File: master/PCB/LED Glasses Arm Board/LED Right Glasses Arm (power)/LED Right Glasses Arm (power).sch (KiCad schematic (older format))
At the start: 24 parts, among them J1 Conn_01x02_Male, J2 Conn_01x01_Male, J3 Conn_01x01_Male, Q1 TP0610T, SW1 SW_SPST, U1 TPS63060

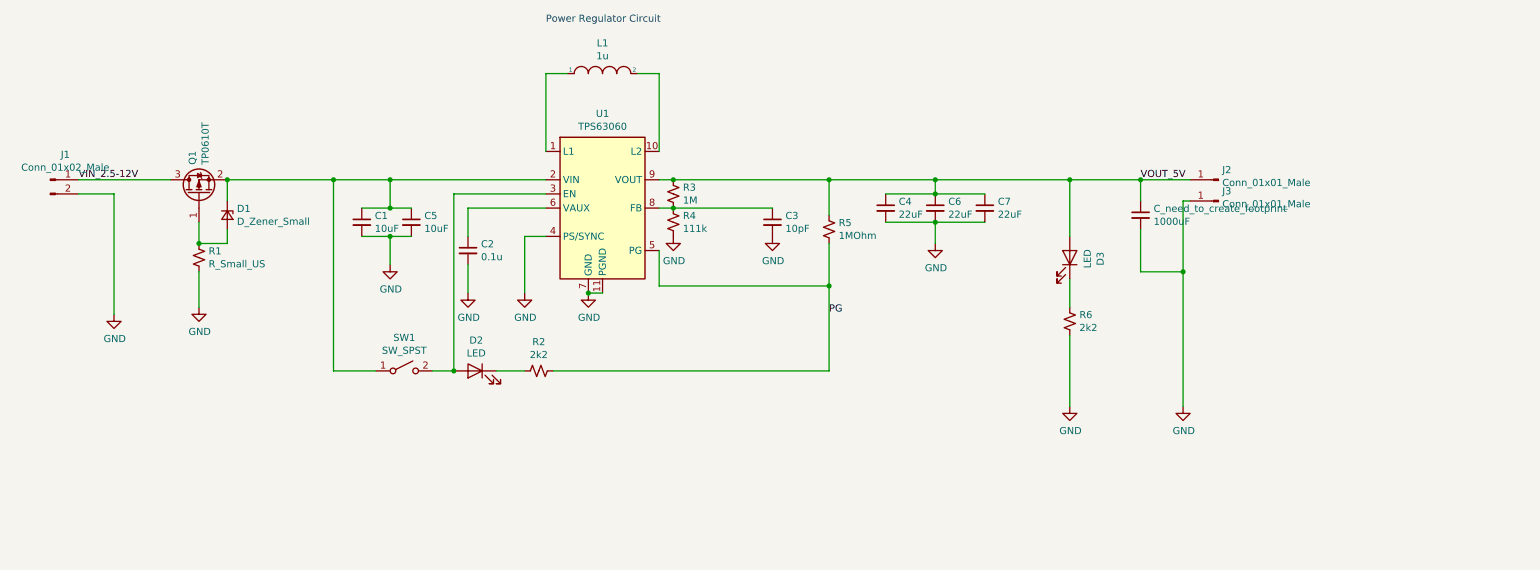
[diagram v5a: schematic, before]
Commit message: PCB update
Changed mosfet, started to route signals
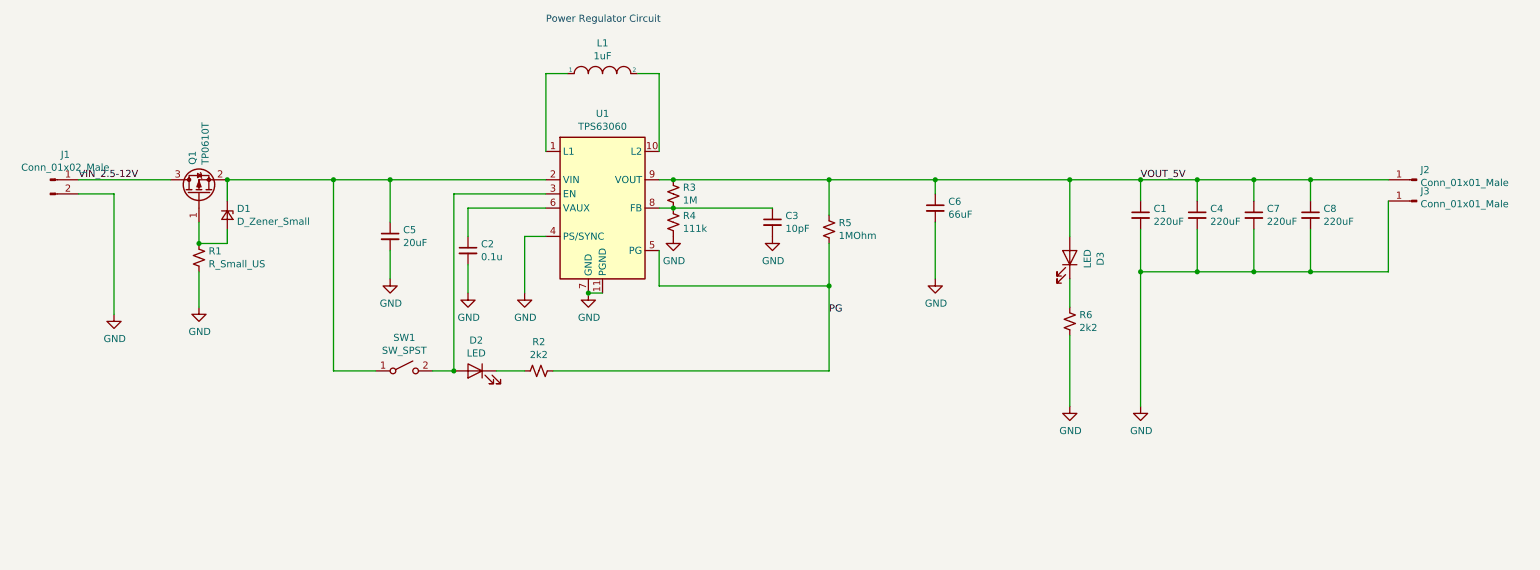
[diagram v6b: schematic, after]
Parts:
- removed C1: 10uF, Capacitor_SMD:C_0603_1608Metric, symbol Device:C_Small
- added C8: 220uF, Capacitor_SMD:C_1206_3216Metric, symbol Device:C_Small
- C1: renamed from C_need_to_create_footprint; value 1000uF -> 220uF; footprint Capacitor_SMD:C_0603_1608Metric -> Capacitor_SMD:C_1206_3216Metric; Link https://www.digikey.com.au/product-detail/en/vishay-sprague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 -> https://au.element14.com/murata/grm31cr60j227me11l/cap-220-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
- C4, C7: value 22uF -> 220uF; footprint Capacitor_SMD:C_0603_1608Metric -> Capacitor_SMD:C_1206_3216Metric; Link (none) -> https://au.element14.com/murata/grm31cr60j227me11l/cap-220-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
- C5: value 10uF -> 20uF
- C6: value 22uF -> 66uF
- J1: footprint Connector_JST:JST_PH_S2B-PH-K_1x02_P2.00mm_Horizontal -> Connector_JST:JST_PH_S2B-PH-SM4-TB_1x02-1MP_P2.00mm_Horizontal; Link (none) -> https://au.element14.com/jst-japan-solderless-terminals/s2b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
- L1: value 1u -> 1uF; Link (none) -> XFL4020-102MEC
- Q1: Link (none) -> https://au.element14.com/vishay/si2315bds-t1-ge3/p-channel-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
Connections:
- net GND: now also C8.2
- net VOUT_5V: now also C8.1
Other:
- moved on the sheet: C5, J2, J3
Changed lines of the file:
@@
-$EndComp
-$Comp
-L Device:C_Small C1
-U 1 1 5F4B72C8
-P 3050 4350
-F 0 "C1" H 3142 4396 50  0000 L CNN
-F 1 "10uF" H 3142 4305 50  0000 L CNN
-F 2 "Capacitor_SMD:C_0603_1608Metric" H 3050 4350 50  0001 C CNN
-F 3 "~" H 3050 4350 50  0001 C CNN
-	1    3050 4350
-	1    0    0    -1
 $EndComp
 $Comp
@@
 P 4750 3300
 F 0 "L1" H 4750 3515 50  0000 C CNN
-F 1 "1u" H 4750 3424 50  0000 C CNN
+F 1 "1uF" H 4750 3424 50  0000 C CNN
 F 2 "Inductor_SMD:L_Coilcraft_XxL4020" H 4750 3300 50  0001 C CNN
-F 3 "~" H 4750 3300 50  0001 C CNN
+F 3 "http://www.farnell.com/datasheets/1682010.pdf" H 4750 3300 50  0001 C CNN
+F 4 "XFL4020-102MEC" H 4750 3300 50  0001 C CNN "Link"
 	1    4750 3300
 	1    0    0    -1
@@
 Connection ~ 6350 4050
 $Comp
-L Device:C_Small C4
-U 1 1 5F4BC943
-P 6750 4250
-F 0 "C4" H 6842 4296 50  0000 L CNN
-F 1 "22uF" H 6842 4205 50  0000 L CNN
-F 2 "Capacitor_SMD:C_0603_1608Metric" H 6750 4250 50  0001 C CNN
-F 3 "~" H 6750 4250 50  0001 C CNN
-	1    6750 4250
-	1    0    0    -1
-$EndComp
-$Comp
 L power:GND #PWR0108
 U 1 1 5F4BEA89
-P 7100 4500
-F 0 "#PWR0108" H 7100 4250 50  0001 C CNN
-F 1 "GND" H 7105 4327 50  0000 C CNN
-F 2 "" H 7100 4500 50  0001 C CNN
-F 3 "" H 7100 4500 50  0001 C CNN
-	1    7100 4500
+P 7100 4750
+F 0 "#PWR0108" H 7100 4500 50  0001 C CNN
+F 1 "GND" H 7105 4577 50  0000 C CNN
+F 2 "" H 7100 4750 50  0001 C CNN
+F 3 "" H 7100 4750 50  0001 C CNN
+	1    7100 4750
 	1    0    0    -1
 $EndComp
@@
 F 1 "TP0610T" H 2106 4105 50  0000 L CNN
 F 2 "Package_TO_SOT_SMD:SOT-23" H 2100 4075 50  0001 L CIN
-F 3 "http://www.vishay.com/docs/70209/70209.pdf" H 1900 4150 50  0001 L CNN
+F 3 "http://www.farnell.com/datasheets/2046951.pdf" H 1900 4150 50  0001 L CNN
+F 4 "https://au.element14.com/vishay/si2315bds-t1-ge3/p-channel-mosfet/dp/1867177?st=p%20channel%20mosfet" H 1900 4150 50  0001 C CNN "Link"
 	1    1900 4150
 	0    -1   -1   0
@@
 L Device:C_Small C5
 U 1 1 604D825D
-P 3400 4350
-F 0 "C5" H 3492 4396 50  0000 L CNN
-F 1 "10uF" H 3492 4305 50  0000 L CNN
-F 2 "Capacitor_SMD:C_0603_1608Metric" H 3400 4350 50  0001 C CNN
-F 3 "~" H 3400 4350 50  0001 C CNN
-	1    3400 4350
+P 3250 4450
+F 0 "C5" H 3342 4496 50  0000 L CNN
+F 1 "20uF" H 3342 4405 50  0000 L CNN
+F 2 "Capacitor_SMD:C_0603_1608Metric" H 3250 4450 50  0001 C CNN
+F 3 "~" H 3250 4450 50  0001 C CNN
+	1    3250 4450
 	1    0    0    -1
 $EndComp
@@
 Wire Wire Line
 	8050 4050 8550 4050
-$Comp
-L Device:C_Small C7
-U 1 1 604E036B
-P 7450 4250
-F 0 "C7" H 7542 4296 50  0000 L CNN
-F 1 "22uF" H 7542 4205 50  0000 L CNN
-F 2 "Capacitor_SMD:C_0603_1608Metric" H 7450 4250 50  0001 C CNN
-F 3 "~" H 7450 4250 50  0001 C CNN
-	1    7450 4250
-	1    0    0    -1
-$EndComp
 $Comp
 L Device:C_Small C6
@@
 P 7100 4250
 F 0 "C6" H 7192 4296 50  0000 L CNN
-F 1 "22uF" H 7192 4205 50  0000 L CNN
+F 1 "66uF" H 7192 4205 50  0000 L CNN
 F 2 "Capacitor_SMD:C_0603_1608Metric" H 7100 4250 50  0001 C CNN
 F 3 "~" H 7100 4250 50  0001 C CNN
@@
 Wire Wire Line
 	7100 4050 8050 4050
-Wire Wire Line
-	7100 4350 7100 4500
 $Comp
 L Connector:Conn_01x02_Male J1
@@
 F 0 "J1" H 956 4228 50  0000 C CNN
 F 1 "Conn_01x02_Male" H 956 4137 50  0000 C CNN
-F 2 "Connector_JST:JST_PH_S2B-PH-K_1x02_P2.00mm_Horizontal" H 850 4050 50  0001 C CNN
-F 3 "~" H 850 4050 50  0001 C CNN
+F 2 "Connector_JST:JST_PH_S2B-PH-SM4-TB_1x02-1MP_P2.00mm_Horizontal" H 850 4050 50  0001 C CNN
+F 3 "http://www.farnell.com/datasheets/1699381.pdf" H 850 4050 50  0001 C CNN
+F 4 "https://au.element14.com/jst-japan-solderless-terminals/s2b-ph-sm4-tb-lf-sn/connector-header-smt-r-a-2mm-2way/dp/9492615" H 850 4050 50  0001 C CNN "Link"
 	1    850  4050
 	1    0    0    -1
@@
 L Connector:Conn_01x01_Male J2
 U 1 1 604D92F9
-P 9100 4050
-F 0 "J2" H 9073 3980 50  0000 R CNN
-F 1 "Conn_01x01_Male" H 9073 4071 50  0000 R CNN
-F 2 "Connector_PinHeader_1.00mm:PinHeader_1x01_P1.00mm_Vertical_SMD_CUSTOM" H 9100 4050 50  0001 C CNN
-F 3 "~" H 9100 4050 50  0001 C CNN
-	1    9100 4050
+P 10500 4050
+F 0 "J2" H 10473 3980 50  0000 R CNN
+F 1 "Conn_01x01_Male" H 10473 4071 50  0000 R CNN
+F 2 "Connector_PinHeader_1.00mm:PinHeader_1x01_P1.00mm_Vertical_SMD_CUSTOM" H 10500 4050 50  0001 C CNN
+F 3 "~" H 10500 4050 50  0001 C CNN
+	1    10500 4050
 	-1   0    0    1
 $EndComp
@@
 L power:GND #PWR0111
 U 1 1 604DB74C
-P 8850 5650
-F 0 "#PWR0111" H 8850 5400 50  0001 C CNN
-F 1 "GND" H 8855 5477 50  0000 C CNN
-F 2 "" H 8850 5650 50  0001 C CNN
-F 3 "" H 8850 5650 50  0001 C CNN
-	1    8850 5650
+P 8550 5650
+F 0 "#PWR0111" H 8550 5400 50  0001 C CNN
+F 1 "GND" H 8555 5477 50  0000 C CNN
+F 2 "" H 8550 5650 50  0001 C CNN
+F 3 "" H 8550 5650 50  0001 C CNN
+	1    8550 5650
 	1    0    0    -1
 $EndComp
@@
 L Connector:Conn_01x01_Male J3
 U 1 1 604DC290
-P 9100 4200
-F 0 "J3" H 9073 4130 50  0000 R CNN
-F 1 "Conn_01x01_Male" H 9073 4221 50  0000 R CNN
-F 2 "Connector_PinHeader_1.00mm:PinHeader_1x01_P1.00mm_Vertical_SMD_CUSTOM" H 9100 4200 50  0001 C CNN
-F 3 "~" H 9100 4200 50  0001 C CNN
-	1    9100 4200
+P 10500 4200
+F 0 "J3" H 10473 4130 50  0000 R CNN
+F 1 "Conn_01x01_Male" H 10473 4221 50  0000 R CNN
+F 2 "Connector_PinHeader_1.00mm:PinHeader_1x01_P1.00mm_Vertical_SMD_CUSTOM" H 10500 4200 50  0001 C CNN
+F 3 "~" H 10500 4200 50  0001 C CNN
+	1    10500 4200
 	-1   0    0    1
 $EndComp
 Wire Wire Line
-	8900 4200 8850 4200
-Wire Wire Line
-	8850 4200 8850 4700
-Wire Wire Line
-	3050 4250 3250 4250
-Connection ~ 3250 4250
-Wire Wire Line
-	3250 4250 3400 4250
-Wire Wire Line
 	2850 4050 3250 4050
-Wire Wire Line
-	3050 4450 3250 4450
 $Comp
 L power:GND #PWR0103
 U 1 1 5F4B6F97
-P 3250 4650
-F 0 "#PWR0103" H 3250 4400 50  0001 C CNN
-F 1 "GND" H 3255 4477 50  0000 C CNN
-F 2 "" H 3250 4650 50  0001 C CNN
-F 3 "" H 3250 4650 50  0001 C CNN
-	1    3250 4650
-	1    0    0    -1
-$EndComp
-Wire Wire Line
-	3250 4050 3250 4250
+P 3250 4750
+F 0 "#PWR0103" H 3250 4500 50  0001 C CNN
+F 1 "GND" H 3255 4577 50  0000 C CNN
+F 2 "" H 3250 4750 50  0001 C CNN
+F 3 "" H 3250 4750 50  0001 C CNN
+	1    3250 4750
+	1    0    0    -1
+$EndComp
 Connection ~ 3250 4050
 Wire Wire Line
 	3250 4050 4350 4050
 Wire Wire Line
-	3250 4450 3250 4650
-Connection ~ 3250 4450
-Wire Wire Line
-	3250 4450 3400 4450
-Wire Wire Line
-	6750 4350 7100 4350
-Connection ~ 7100 4350
-Wire Wire Line
-	7100 4350 7450 4350
-Wire Wire Line
-	6750 4150 7100 4150
-Connection ~ 7100 4150
-Wire Wire Line
-	7100 4150 7450 4150
-$Comp
-L Device:C_Small C_need_to_create_footprint
+	3250 4550 3250 4750
+$Comp
+L Device:C_Small C1
 U 1 1 60505078
 P 8550 4300
-F 0 "C_need_to_create_footprint" H 8642 4346 50  0000 L CNN
-F 1 "1000uF" H 8642 4255 50  0000 L CNN
-F 2 "Capacitor_SMD:C_0603_1608Metric" H 8550 4300 50  0001 C CNN
-F 3 "https://www.vishay.com/docs/40012/591d.pdf" H 8550 4300 50  0001 C CNN
-F 4 "https://www.digikey.com.au/product-detail/en/vishay-sprague/591D108X96R3R2T20H/718-1619-1-ND/1973897" H 8550 4300 50  0001 C CNN "Link"
+F 0 "C1" H 8642 4346 50  0000 L CNN
+F 1 "220uF" H 8642 4255 50  0000 L CNN
+F 2 "Capacitor_SMD:C_1206_3216Metric" H 8550 4300 50  0001 C CNN
+F 3 "http://www.farnell.com/datasheets/2867879.pdf" H 8550 4300 50  0001 C CNN
+F 4 "https://au.element14.com/murata/grm31cr60j227me11l/cap-220-f-6-3v-20-x5r-1206/dp/2494472" H 8550 4300 50  0001 C CNN "Link"
 	1    8550 4300
 	1    0    0    -1
@@
 Connection ~ 8550 4050
 Wire Wire Line
-	8550 4050 8900 4050
-Wire Wire Line
 	8550 4400 8550 4700
 Wire Wire Line
-	8550 4700 8850 4700
-Connection ~ 8850 4700
-Wire Wire Line
-	8850 4700 8850 5650
+	8550 4700 8550 5650
+Wire Wire Line
+	3250 4050 3250 4350
+Wire Wire Line
+	7100 4350 7100 4750
+Wire Wire Line
+	10300 4700 10300 4200
+Connection ~ 8550 4700
+$Comp
+L Device:C_Small C4
+U 1 1 60562E44
+P 8950 4300
+F 0 "C4" H 9042 4346 50  0000 L CNN
+F 1 "220uF" H 9042 4255 50  0000 L CNN
+F 2 "Capacitor_SMD:C_1206_3216Metric" H 8950 4300 50  0001 C CNN
+F 3 "http://www.farnell.com/datasheets/2867879.pdf" H 8950 4300 50  0001 C CNN
+F 4 "https://au.element14.com/murata/grm31cr60j227me11l/cap-220-f-6-3v-20-x5r-1206/dp/2494472" H 8950 4300 50  0001 C CNN "Link"
+	1    8950 4300
+	1    0    0    -1
+$EndComp
+$Comp
+L Device:C_Small C7
+U 1 1 605639D8
+P 9350 4300
+F 0 "C7" H 9442 4346 50  0000 L CNN
+F 1 "220uF" H 9442 4255 50  0000 L CNN
+F 2 "Capacitor_SMD:C_1206_3216Metric" H 9350 4300 50  0001 C CNN
+F 3 "http://www.farnell.com/datasheets/2867879.pdf" H 9350 4300 50  0001 C CNN
+F 4 "https://au.element14.com/murata/grm31cr60j227me11l/cap-220-f-6-3v-20-x5r-1206/dp/2494472" H 9350 4300 50  0001 C CNN "Link"
+	1    9350 4300
+	1    0    0    -1
+$EndComp
+$Comp
+L Device:C_Small C8
+U 1 1 60564591
+P 9750 4300
+F 0 "C8" H 9842 4346 50  0000 L CNN
+F 1 "220uF" H 9842 4255 50  0000 L CNN
+F 2 "Capacitor_SMD:C_1206_3216Metric" H 9750 4300 50  0001 C CNN
+F 3 "http://www.farnell.com/datasheets/2867879.pdf" H 9750 4300 50  0001 C CNN
+F 4 "https://au.element14.com/murata/grm31cr60j227me11l/cap-220-f-6-3v-20-x5r-1206/dp/2494472" H 9750 4300 50  0001 C CNN "Link"
+	1    9750 4300
+	1    0    0    -1
+$EndComp
+Wire Wire Line
+	8550 4700 8950 4700
+Wire Wire Line
+	8550 4050 8950 4050
+Wire Wire Line
+	8950 4200 8950 4050
+Connection ~ 8950 4050
+Wire Wire Line
+	8950 4050 9350 4050
+Wire Wire Line
+	8950 4400 8950 4700
+Connection ~ 8950 4700
+Wire Wire Line
+	8950 4700 9350 4700
+Wire Wire Line
+	9350 4200 9350 4050
+Connection ~ 9350 4050
+Wire Wire Line
+	9350 4050 9750 4050
+Wire Wire Line
+	9750 4200 9750 4050
+Connection ~ 9750 4050
+Wire Wire Line
+	9750 4050 10300 4050
+Wire Wire Line
+	9350 4400 9350 4700
+Connection ~ 9350 4700
+Wire Wire Line
+	9350 4700 9750 4700
+Wire Wire Line
+	9750 4400 9750 4700
+Connection ~ 9750 4700
+Wire Wire Line
+	9750 4700 10300 4700
 $EndSCHEMATC

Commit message: added a few more links to products
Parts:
- J1: Digikey Link (none) -> https://www.digikey.com.au/product-detail/en/jst-sales-amer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
- L1: element14 (none) -> https://au.element14.com/coilcraft/xfl4020-102mec/inductor-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
- Q1: Digikey Link (none) -> https://www.digikey.com.au/product-detail/en/vishay-silicon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
- R3, R5: Digikey Link (none) -> https://www.digikey.com.au/product-detail/en/yageo/RT0603BR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
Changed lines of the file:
@@
 F 3 "http://www.farnell.com/datasheets/1682010.pdf" H 4750 3300 50  0001 C CNN
 F 4 "XFL4020-102MEC" H 4750 3300 50  0001 C CNN "Link"
+F 5 "https://au.element14.com/coilcraft/xfl4020-102mec/inductor-1uh-11a-20-pwr-64mhz/dp/2289214?st=xfl4020-102mec" H 4750 3300 50  0001 C CNN "element14"
 	1    4750 3300
 	1    0    0    -1
@@
 F 2 "Resistor_SMD:R_0603_1608Metric" H 5250 4150 50  0001 C CNN
 F 3 "~" H 5250 4150 50  0001 C CNN
+F 4 "https://www.digikey.com.au/product-detail/en/yageo/RT0603BRD071ML/YAG4498CT-ND/6616654" H 5250 4150 50  0001 C CNN "Digikey Link"
 	1    5250 4150
 	1    0    0    -1
@@
 F 2 "Resistor_SMD:R_0603_1608Metric" H 6350 4400 50  0001 C CNN
 F 3 "~" H 6350 4400 50  0001 C CNN
+F 4 "https://www.digikey.com.au/product-detail/en/yageo/RT0603BRD071ML/YAG4498CT-ND/6616654" H 6350 4400 50  0001 C CNN "Digikey Link"
 	1    6350 4400
 	1    0    0    -1
@@
 F 3 "http://www.farnell.com/datasheets/2046951.pdf" H 1900 4150 50  0001 L CNN
 F 4 "https://au.element14.com/vishay/si2315bds-t1-ge3/p-channel-mosfet/dp/1867177?st=p%20channel%20mosfet" H 1900 4150 50  0001 C CNN "Link"
+F 5 "https://www.digikey.com.au/product-detail/en/vishay-siliconix/SI2315BDS-T1-GE3/SI2315BDS-T1-GE3CT-ND/6595280" H 1900 4150 50  0001 C CNN "Digikey Link"
 	1    1900 4150
 	0    -1   -1   0
@@
 F 3 "http://www.farnell.com/datasheets/1699381.pdf" H 850 4050 50  0001 C CNN
 F 4 "https://au.element14.com/jst-japan-solderless-terminals/s2b-ph-sm4-tb-lf-sn/connector-header-smt-r-a-2mm-2way/dp/9492615" H 850 4050 50  0001 C CNN "Link"
+F 5 "https://www.digikey.com.au/product-detail/en/jst-sales-america-inc/S2B-PH-SM4-TB-LF-SN/455-1749-2-ND/926655" H 850 4050 50  0001 C CNN "Digikey Link"
 	1    850  4050
 	1    0    0    -1
